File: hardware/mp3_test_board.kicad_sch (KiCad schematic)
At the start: 0 parts

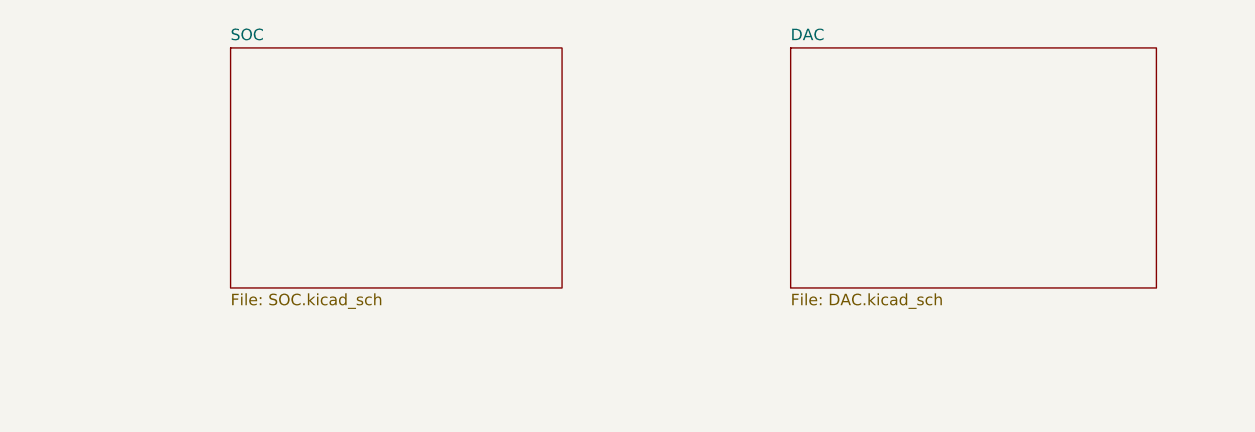
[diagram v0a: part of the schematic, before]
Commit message: added hierarchy labels
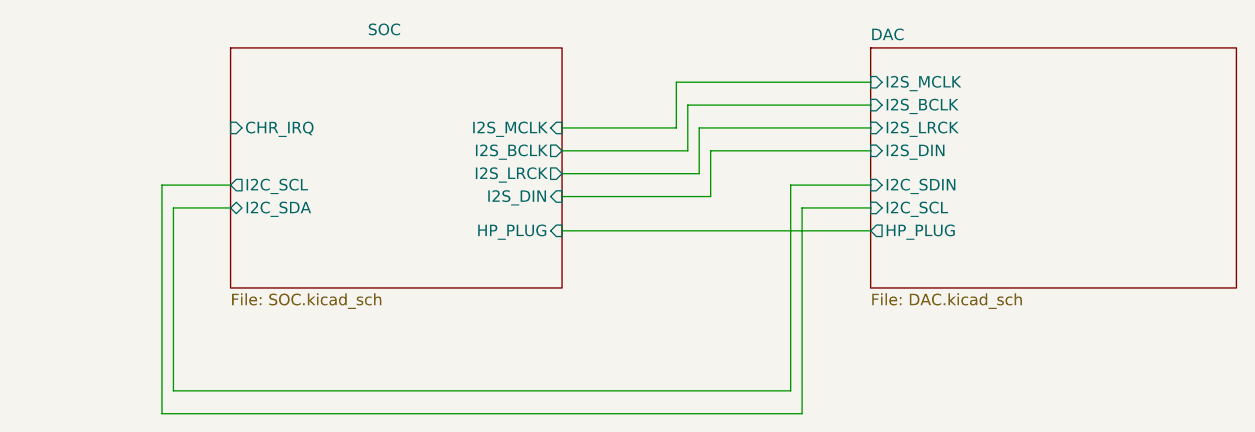
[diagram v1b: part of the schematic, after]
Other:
- sheet DAC ports: added HP_PLUG, I2C_SCL, I2C_SDIN, I2S_BCLK, I2S_DIN, I2S_LRCK, I2S_MCLK; removed none
- sheet SOC ports: added CHR_IRQ, HP_PLUG, I2C_SCL, I2C_SDA, I2S_BCLK, I2S_DIN, I2S_LRCK, I2S_MCLK; removed none
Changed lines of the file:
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@@
 (kicad_sch (version 20211123) (generator eeschema)
   (paper "A4")
-  (sheet (at 185.42 69.85) (size 40.64 26.67) (fields_autoplaced)
+  (wire (pts (xy 115.57 85.09) (xy 115.57 110.49))
+    (stroke (width 0) (type default) (color 0 0 0 0))
+  )
+  (wire (pts (xy 160.02 86.36) (xy 176.53 86.36))
+    (stroke (width 0) (type default) (color 0 0 0 0))
+  )
+  (wire (pts (xy 186.69 110.49) (xy 186.69 87.63))
+    (stroke (width 0) (type default) (color 0 0 0 0))
+  )
+  (wire (pts (xy 185.42 107.95) (xy 185.42 85.09))
+    (stroke (width 0) (type default) (color 0 0 0 0))
+  )
+  (wire (pts (xy 173.99 81.28) (xy 173.99 76.2))
+    (stroke (width 0) (type default) (color 0 0 0 0))
+  )
+  (wire (pts (xy 175.26 78.74) (xy 194.31 78.74))
+    (stroke (width 0) (type default) (color 0 0 0 0))
+  )
+  (wire (pts (xy 175.26 83.82) (xy 175.26 78.74))
+    (stroke (width 0) (type default) (color 0 0 0 0))
+  )
+  (wire (pts (xy 172.72 73.66) (xy 194.31 73.66))
+    (stroke (width 0) (type default) (color 0 0 0 0))
+  )
+  (wire (pts (xy 185.42 85.09) (xy 194.31 85.09))
+    (stroke (width 0) (type default) (color 0 0 0 0))
+  )
+  (wire (pts (xy 116.84 87.63) (xy 116.84 107.95))
+    (stroke (width 0) (type default) (color 0 0 0 0))
+  )
+  (wire (pts (xy 160.02 90.17) (xy 194.31 90.17))
+    (stroke (width 0) (type default) (color 0 0 0 0))
+  )
+  (wire (pts (xy 186.69 87.63) (xy 194.31 87.63))
+    (stroke (width 0) (type default) (color 0 0 0 0))
+  )
+  (wire (pts (xy 160.02 81.28) (xy 173.99 81.28))
+    (stroke (width 0) (type default) (color 0 0 0 0))
+  )
+  (wire (pts (xy 160.02 83.82) (xy 175.26 83.82))
+    (stroke (width 0) (type default) (color 0 0 0 0))
+  )
+  (wire (pts (xy 123.19 85.09) (xy 115.57 85.09))
+    (stroke (width 0) (type default) (color 0 0 0 0))
+  )
+  (wire (pts (xy 123.19 87.63) (xy 116.84 87.63))
+    (stroke (width 0) (type default) (color 0 0 0 0))
+  )
+  (wire (pts (xy 172.72 78.74) (xy 172.72 73.66))
+    (stroke (width 0) (type default) (color 0 0 0 0))
+  )
+  (wire (pts (xy 115.57 110.49) (xy 186.69 110.49))
+    (stroke (width 0) (type default) (color 0 0 0 0))
+  )
+  (wire (pts (xy 173.99 76.2) (xy 194.31 76.2))
+    (stroke (width 0) (type default) (color 0 0 0 0))
+  )
+  (wire (pts (xy 176.53 81.28) (xy 194.31 81.28))
+    (stroke (width 0) (type default) (color 0 0 0 0))
+  )
+  (wire (pts (xy 116.84 107.95) (xy 185.42 107.95))
+    (stroke (width 0) (type default) (color 0 0 0 0))
+  )
+  (wire (pts (xy 176.53 86.36) (xy 176.53 81.28))
+    (stroke (width 0) (type default) (color 0 0 0 0))
+  )
+  (wire (pts (xy 160.02 78.74) (xy 172.72 78.74))
+    (stroke (width 0) (type default) (color 0 0 0 0))
+  )
+  (sheet (at 194.31 69.85) (size 40.64 26.67) (fields_autoplaced)
     (stroke (width 0.1524) (type solid) (color 0 0 0 0))
     (fill (color 0 0 0 0.0000))
-    (property "Sheet name" "DAC" (id 0) (at 185.42 69.1384 0)
+    (property "Sheet name" "DAC" (id 0) (at 194.31 69.1384 0)
       (effects (font (size 1.27 1.27)) (justify left bottom))
     )
-    (property "Sheet file" "DAC.kicad_sch" (id 1) (at 185.42 97.1046 0)
+    (property "Sheet file" "DAC.kicad_sch" (id 1) (at 194.31 97.1046 0)
       (effects (font (size 1.27 1.27)) (justify left top))
     )
-  )
-  (sheet (at 123.19 69.85) (size 36.83 26.67) (fields_autoplaced)
+    (pin "HP_PLUG" output (at 194.31 90.17 180)
+      (effects (font (size 1.27 1.27)) (justify left))
+    )
+    (pin "I2C_SCL" input (at 194.31 87.63 180)
+      (effects (font (size 1.27 1.27)) (justify left))
+    )
+    (pin "I2C_SDIN" input (at 194.31 85.09 180)
+      (effects (font (size 1.27 1.27)) (justify left))
+    )
+    (pin "I2S_LRCK" input (at 194.31 78.74 180)
+      (effects (font (size 1.27 1.27)) (justify left))
+    )
+    (pin "I2S_DIN" input (at 194.31 81.28 180)
+      (effects (font (size 1.27 1.27)) (justify left))
+    )
+    (pin "I2S_BCLK" input (at 194.31 76.2 180)
+      (effects (font (size 1.27 1.27)) (justify left))
+    )
+    (pin "I2S_MCLK" input (at 194.31 73.66 180)
+      (effects (font (size 1.27 1.27)) (justify left))
+    )
+  )
+  (sheet (at 123.19 69.85) (size 36.83 26.67)
     (stroke (width 0.1524) (type solid) (color 0 0 0 0))
     (fill (color 0 0 0 0.0000))
-    (property "Sheet name" "SOC" (id 0) (at 123.19 69.1384 0)
+    (property "Sheet name" "SOC" (id 0) (at 138.43 68.58 0)
       (effects (font (size 1.27 1.27)) (justify left bottom))
     )
     (property "Sheet file" "SOC.kicad_sch" (id 1) (at 123.19 97.1046 0)
       (effects (font (size 1.27 1.27)) (justify left top))
+    )
+    (pin "I2S_MCLK" input (at 160.02 78.74 0)
+      (effects (font (size 1.27 1.27)) (justify right))
+    )
+    (pin "I2S_BCLK" output (at 160.02 81.28 0)
+      (effects (font (size 1.27 1.27)) (justify right))
+    )
+    (pin "I2S_LRCK" output (at 160.02 83.82 0)
+      (effects (font (size 1.27 1.27)) (justify right))
+    )
+    (pin "I2S_DIN" input (at 160.02 86.36 0)
+      (effects (font (size 1.27 1.27)) (justify right))
+    )
+    (pin "HP_PLUG" input (at 160.02 90.17 0)
+      (effects (font (size 1.27 1.27)) (justify right))
+    )
+    (pin "CHR_IRQ" input (at 123.19 78.74 180)
+      (effects (font (size 1.27 1.27)) (justify left))
+    )
+    (pin "I2C_SCL" output (at 123.19 85.09 180)
+      (effects (font (size 1.27 1.27)) (justify left))
+    )
+    (pin "I2C_SDA" bidirectional (at 123.19 87.63 180)
+      (effects (font (size 1.27 1.27)) (justify left))
     )
   )
@@
       (reference "#PWR0198") (unit 1) (value "GNDA") (footprint "")
     )
+    (path "/401dcf25-129a-4017-9713-e4979f9d70cf/2aff7937-01c4-404d-a154-0b42c2ccb63c"
+      (reference "#PWR?") (unit 1) (value "+3V3") (footprint "")
+    )
     (path "/e1791f45-9313-4623-bca3-b0a68fdadfbe/ee67da40-1ebe-4920-a137-523a8361865b"
       (reference "C1") (unit 1) (value "C") (footprint "rlib_passive:C_0603_1608Metric")
@@
     )
     (path "/401dcf25-129a-4017-9713-e4979f9d70cf/70d39fec-44ce-4d2e-8442-7a88ed5f8474"
-      (reference "R45") (unit 1) (value "R") (footprint "rlib_passive:R_0603_1608Metric")
+      (reference "R45") (unit 1) (value "10K") (footprint "rlib_passive:R_0603_1608Metric")
     )
     (path "/494fd4b1-1de7-49fe-827f-914491efe850/65e94c21-2429-4262-a530-190e4ac76e48"
@@
       (reference "R47") (unit 1) (value "R") (footprint "rlib_passive:R_0603_1608Metric")
     )
+    (path "/401dcf25-129a-4017-9713-e4979f9d70cf/d0c5e55a-81dd-4f8c-877f-c2655a99520b"
+      (reference "R?") (unit 1) (value "10K") (footprint "")
+    )
     (path "/e1791f45-9313-4623-bca3-b0a68fdadfbe/34008909-d15a-432e-8a83-89239de5595a"

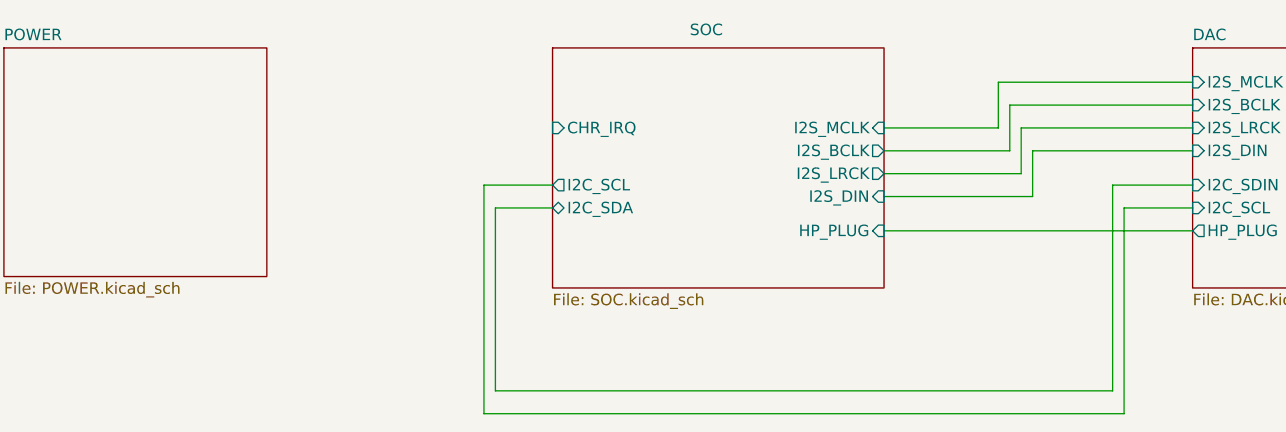
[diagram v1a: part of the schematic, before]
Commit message: added esd protection
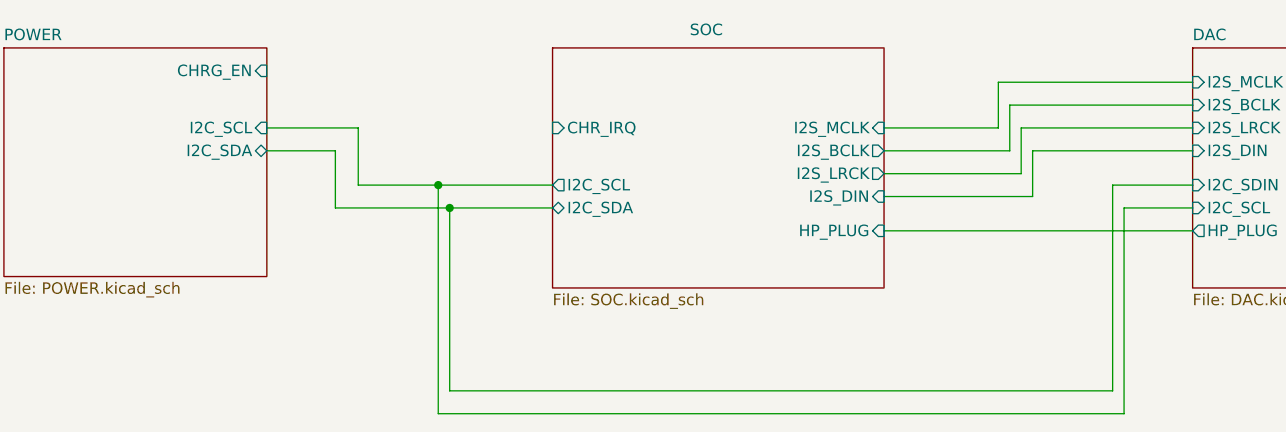
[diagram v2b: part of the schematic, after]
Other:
- sheet POWER ports: added CHRG_EN, I2C_SCL, I2C_SDA; removed none
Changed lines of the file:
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@@
 (kicad_sch (version 20211123) (generator eeschema)
   (paper "A4")
-  (wire (pts (xy 115.57 85.09) (xy 115.57 110.49))
+  (junction (at 110.49 85.09) (diameter 0) (color 0 0 0 0)
+  )
+  (junction (at 111.76 87.63) (diameter 0) (color 0 0 0 0)
+  )
+  (wire (pts (xy 110.49 85.09) (xy 110.49 110.49))
     (stroke (width 0) (type default) (color 0 0 0 0))
   )
@@
     (stroke (width 0) (type default) (color 0 0 0 0))
   )
+  (wire (pts (xy 99.06 81.28) (xy 99.06 87.63))
+    (stroke (width 0) (type default) (color 0 0 0 0))
+  )
   (wire (pts (xy 173.99 81.28) (xy 173.99 76.2))
     (stroke (width 0) (type default) (color 0 0 0 0))
   )
+  (wire (pts (xy 91.44 78.74) (xy 101.6 78.74))
+    (stroke (width 0) (type default) (color 0 0 0 0))
+  )
   (wire (pts (xy 175.26 78.74) (xy 194.31 78.74))
     (stroke (width 0) (type default) (color 0 0 0 0))
@@
     (stroke (width 0) (type default) (color 0 0 0 0))
   )
-  (wire (pts (xy 116.84 87.63) (xy 116.84 107.95))
+  (wire (pts (xy 101.6 78.74) (xy 101.6 85.09))
+    (stroke (width 0) (type default) (color 0 0 0 0))
+  )
+  (wire (pts (xy 111.76 87.63) (xy 111.76 107.95))
     (stroke (width 0) (type default) (color 0 0 0 0))
   )
@@
     (stroke (width 0) (type default) (color 0 0 0 0))
   )
-  (wire (pts (xy 123.19 85.09) (xy 115.57 85.09))
-    (stroke (width 0) (type default) (color 0 0 0 0))
-  )
-  (wire (pts (xy 123.19 87.63) (xy 116.84 87.63))
+  (wire (pts (xy 110.49 85.09) (xy 123.19 85.09))
+    (stroke (width 0) (type default) (color 0 0 0 0))
+  )
+  (wire (pts (xy 111.76 87.63) (xy 123.19 87.63))
     (stroke (width 0) (type default) (color 0 0 0 0))
   )
@@
     (stroke (width 0) (type default) (color 0 0 0 0))
   )
-  (wire (pts (xy 115.57 110.49) (xy 186.69 110.49))
+  (wire (pts (xy 91.44 81.28) (xy 99.06 81.28))
+    (stroke (width 0) (type default) (color 0 0 0 0))
+  )
+  (wire (pts (xy 110.49 110.49) (xy 186.69 110.49))
+    (stroke (width 0) (type default) (color 0 0 0 0))
+  )
+  (wire (pts (xy 99.06 87.63) (xy 111.76 87.63))
+    (stroke (width 0) (type default) (color 0 0 0 0))
+  )
+  (wire (pts (xy 101.6 85.09) (xy 110.49 85.09))
     (stroke (width 0) (type default) (color 0 0 0 0))
   )
@@
     (stroke (width 0) (type default) (color 0 0 0 0))
   )
-  (wire (pts (xy 116.84 107.95) (xy 185.42 107.95))
+  (wire (pts (xy 111.76 107.95) (xy 185.42 107.95))
     (stroke (width 0) (type default) (color 0 0 0 0))
   )
@@
       (effects (font (size 1.27 1.27)) (justify left top))
     )
+    (pin "CHRG_EN" input (at 91.44 72.39 0)
+      (effects (font (size 1.27 1.27)) (justify right))
+    )
+    (pin "I2C_SCL" input (at 91.44 78.74 0)
+      (effects (font (size 1.27 1.27)) (justify right))
+    )
+    (pin "I2C_SDA" bidirectional (at 91.44 81.28 0)
+      (effects (font (size 1.27 1.27)) (justify right))
+    )
   )
   (sheet_instances
@@
       (reference "#PWR0198") (unit 1) (value "GNDA") (footprint "")
     )
+    (path "/401dcf25-129a-4017-9713-e4979f9d70cf/0b716140-997f-4184-89d2-783963198e90"
+      (reference "#PWR?") (unit 1) (value "GNDA") (footprint "")
+    )
     (path "/401dcf25-129a-4017-9713-e4979f9d70cf/2aff7937-01c4-404d-a154-0b42c2ccb63c"
       (reference "#PWR?") (unit 1) (value "+3V3") (footprint "")
     )
+    (path "/494fd4b1-1de7-49fe-827f-914491efe850/84e98b4c-029c-4e3f-8234-3d5ae1b7c3bf"
+      (reference "#PWR?") (unit 1) (value "GND") (footprint "")
+    )
+    (path "/e1791f45-9313-4623-bca3-b0a68fdadfbe/c8d76f40-3018-4afd-96d9-b418f6c3c2c8"
+      (reference "#PWR?") (unit 1) (value "GND") (footprint "")
+    )
     (path "/e1791f45-9313-4623-bca3-b0a68fdadfbe/ee67da40-1ebe-4920-a137-523a8361865b"
       (reference "C1") (unit 1) (value "C") (footprint "rlib_passive:C_0603_1608Metric")
@@
       (reference "C77") (unit 1) (value "C") (footprint "rlib_passive:C_0603_1608Metric")
     )
+    (path "/e1791f45-9313-4623-bca3-b0a68fdadfbe/5ff4f9c2-a000-4b95-9a23-fb27c4f6b3df"
+      (reference "C?") (unit 1) (value "C") (footprint "rlib_passive:C_0603_1608Metric")
+    )
+    (path "/494fd4b1-1de7-49fe-827f-914491efe850/1abe6b1e-386f-4c57-92af-3574bc5007e5"
+      (reference "D?") (unit 1) (value "PESD3V3L1BA") (footprint "rlib_passive:D_SOD-323F")
+    )
+    (path "/401dcf25-129a-4017-9713-e4979f9d70cf/41c5468a-7b29-4a02-89d4-8289276e9665"
+      (reference "D?") (unit 1) (value "PESD3V3L1BA") (footprint "rlib_passive:D_SOD-323F")
+    )
+    (path "/401dcf25-129a-4017-9713-e4979f9d70cf/99027239-2fb6-4bc8-bdb8-21735707998d"
+      (reference "D?") (unit 1) (value "PESD3V3L1BA") (footprint "rlib_passive:D_SOD-323F")
+    )
+    (path "/494fd4b1-1de7-49fe-827f-914491efe850/af8f7198-3a33-4b75-b19c-e2105d6136be"
+      (reference "D?") (unit 1) (value "PESD3V3L1BA") (footprint "rlib_passive:D_SOD-323F")
+    )
+    (path "/494fd4b1-1de7-49fe-827f-914491efe850/b676d5a7-9f8a-42d9-9242-5310b46daa9a"
+      (reference "D?") (unit 1) (value "PESD3V3L1BA") (footprint "rlib_passive:D_SOD-323F")
+    )
+    (path "/494fd4b1-1de7-49fe-827f-914491efe850/cd24cc6b-f34f-4fa8-bf71-71e3e22b95aa"
+      (reference "D?") (unit 1) (value "PESD3V3L1BA") (footprint "rlib_passive:D_SOD-323F")
+    )
+    (path "/e1791f45-9313-4623-bca3-b0a68fdadfbe/d6244fd8-714f-4102-a06e-12a381d507e1"
+      (reference "D?") (unit 1) (value "PESD3V3L1BA") (footprint "rlib_passive:D_SOD-323F")
+    )
+    (path "/494fd4b1-1de7-49fe-827f-914491efe850/e6cf5096-8d43-47e9-99b5-a989db6250a9"
+      (reference "D?") (unit 1) (value "PESD3V3L1BA") (footprint "rlib_passive:D_SOD-323F")
+    )
+    (path "/494fd4b1-1de7-49fe-827f-914491efe850/f49017c2-888d-4f92-927c-0609f2a8bc0a"
+      (reference "D?") (unit 1) (value "PESD3V3L1BA") (footprint "rlib_passive:D_SOD-323F")
+    )
+    (path "/494fd4b1-1de7-49fe-827f-914491efe850/f8f4c10a-71d4-48ab-9757-957e9a329f08"
+      (reference "D?") (unit 1) (value "PESD3V3L1BA") (footprint "rlib_passive:D_SOD-323F")
+    )
     (path "/e1791f45-9313-4623-bca3-b0a68fdadfbe/e5b51f52-cbdb-41b6-aea2-0bbaf6faed59"
       (reference "F1") (unit 1) (value "Fuse") (footprint "")
@@
       (reference "TP8") (unit 1) (value "TestPoint") (footprint "")
     )
+    (path "/494fd4b1-1de7-49fe-827f-914491efe850/54df205b-2658-4c87-b91d-531281f6bad4"
+      (reference "TP?") (unit 1) (value "TestPoint") (footprint "")
+    )
+    (path "/494fd4b1-1de7-49fe-827f-914491efe850/b21ffa38-3376-4c3e-ac61-29ad715a012e"
+      (reference "TP?") (unit 1) (value "TestPoint") (footprint "")
+    )
     (path "/e1791f45-9313-4623-bca3-b0a68fdadfbe/c6e4eb73-688e-4be1-9b7c-68677c2da41c"

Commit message: sfsf
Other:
- removed sheet DAC
- added sheet NewDAC (NewDAC.kicad_sch)
